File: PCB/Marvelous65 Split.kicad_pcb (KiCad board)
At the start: 2 copper layers, 349.3 x 107.2 mm, 213 parts, among them J1 USB_C_Receptacle_USB2.0, J2 Conn_01x04, J3 AudioJack4, J4 Conn_01x02, J5 USB_C_Receptacle_USB2.0, J6 Conn_01x04, J7 AudioJack4, J8 Conn_01x02, SW1 SW_DPDT_x2, SW2 SW_PUSH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

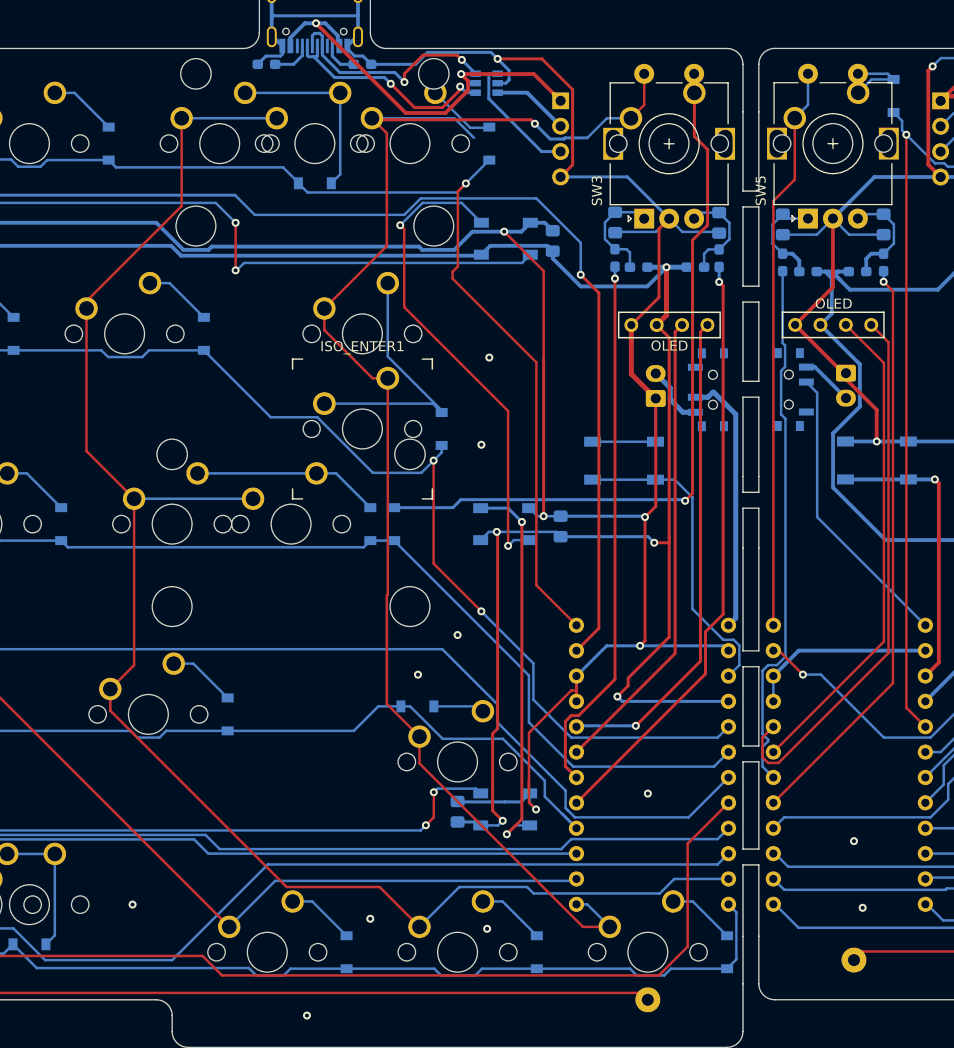
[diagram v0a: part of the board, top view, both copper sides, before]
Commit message: fix iso enter and panelization
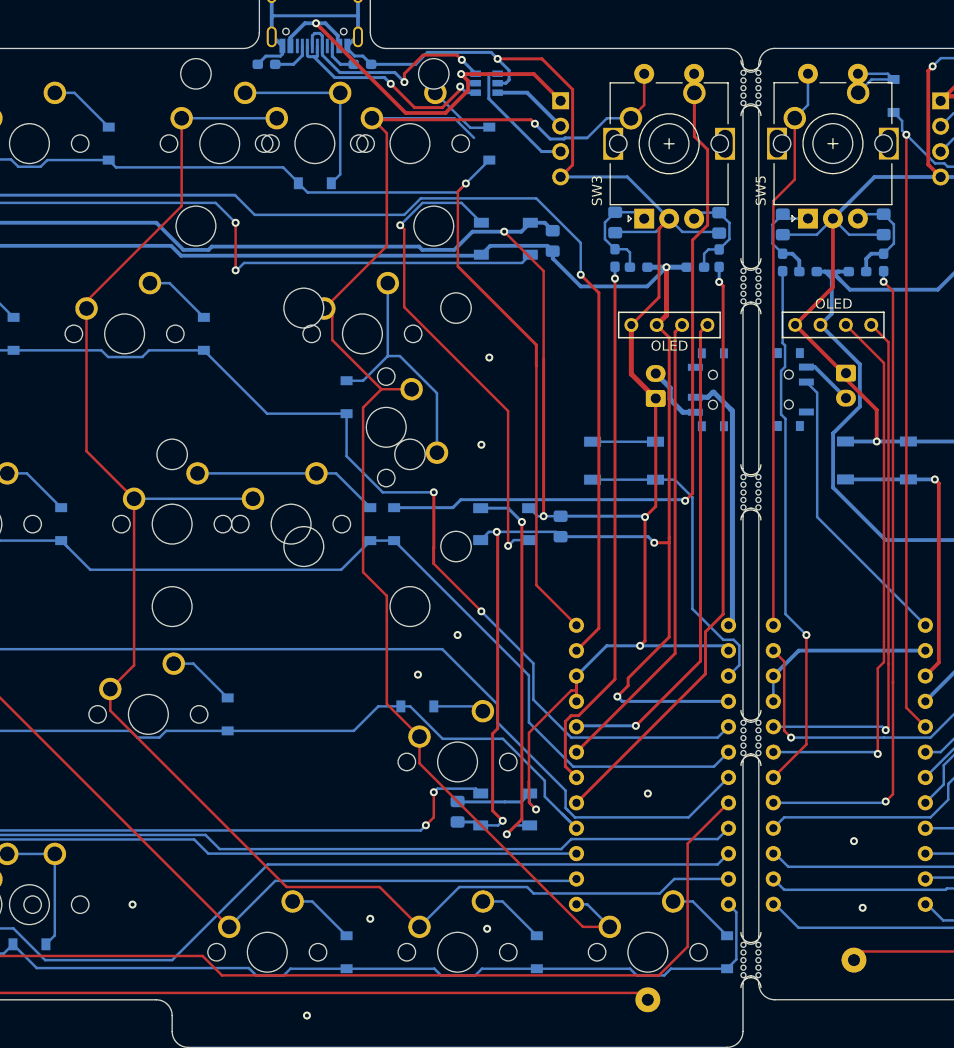
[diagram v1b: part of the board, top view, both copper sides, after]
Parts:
- added mouse-bite-3mm-slot: VAL**, Panelization:mouse-bite-3mm-slot, F.Cu at (-23.4, -114.7)
- added mouse-bite-3mm-slot: VAL**, Panelization:mouse-bite-3mm-slot, F.Cu at (-23.4, -49.6)
- added mouse-bite-3mm-slot: VAL**, Panelization:mouse-bite-3mm-slot, F.Cu at (-23.4, -74.2)
- added mouse-bite-3mm-slot: VAL**, Panelization:mouse-bite-3mm-slot, F.Cu at (-23.4, -94.8)
- added mouse-bite-3mm-slot: VAL**, Panelization:mouse-bite-3mm-slot, F.Cu at (-23.4, -27.4)
- ISO_ENTER1: footprint keyswitches:SW_MX -> MX_Only:MXOnly-ISO-ROTATED-ReversedStabilizers-NoLED
- moved D37 10.0 mm to (-63.9, -83.7)
- moved ISO_ENTER1 2.39 mm to (-59.9, -80.7)
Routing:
- net L_ROT_B: track 58.6 -> 65.2 mm, vias 1 -> 2
- net L_SCL: track 48.9 -> 55.3 mm, vias 0 -> 1
- net L_DATA: track 191.4 -> 196.0 mm
- net ROW2: track 178.2 -> 181.9 mm
- net COL7: track 146.5 -> 149.8 mm
- net Net-(D37-Pad2): track 27.3 -> 24.9 mm
- net ROW1: track 197.7 -> 195.5 mm
- net L_SDA: track 54.5 -> 52.8 mm, vias 0 -> 1
- net L_ROT_A: track 53.5 -> 53.4 mm, vias 0 -> 1
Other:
- outline, holes or cut-outs redrawn

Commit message: updated rendered images
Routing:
- net GND: vias 48 -> 58
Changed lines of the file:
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@@
     (thickness 1.6)
     (drawings 2718)
-    (tracks 1812)
+    (tracks 1822)
     (zones 0)
     (modules 218)
@@
       (padsonsilk false)
       (subtractmaskfromsilk false)
-      (outputformat 1)
+      (outputformat 5)
       (mirror false)
       (drillshape 0)
@@
   (via (at 0.237615 -32.795405) (size 0.8) (drill 0.4) (layers F.Cu B.Cu) (net 2))
   (via (at 5.137615 -50.445405) (size 0.8) (drill 0.4) (layers F.Cu B.Cu) (net 2))
+  (via (at -15.462385 -82.132905) (size 0.8) (drill 0.4) (layers F.Cu B.Cu) (net 2))
+  (via (at -13.081135 -45.620405) (size 0.8) (drill 0.4) (layers F.Cu B.Cu) (net 2))
+  (via (at -31.337385 -48.001655) (size 0.8) (drill 0.4) (layers F.Cu B.Cu) (net 2))
+  (via (at -34.512385 -32.126655) (size 0.8) (drill 0.4) (layers F.Cu B.Cu) (net 2))
+  (via (at -34.512385 -35.301655) (size 0.8) (drill 0.4) (layers F.Cu B.Cu) (net 2))
+  (via (at -34.512385 -38.476655) (size 0.8) (drill 0.4) (layers F.Cu B.Cu) (net 2))
+  (via (at -32.131135 -40.857905) (size 0.8) (drill 0.4) (layers F.Cu B.Cu) (net 2))
+  (via (at 51.212615 -38.476655) (size 0.8) (drill 0.4) (layers F.Cu B.Cu) (net 2))
+  (via (at 21.843865 -55.145405) (size 0.8) (drill 0.4) (layers F.Cu B.Cu) (net 2))
+  (via (at 45.656365 -51.176655) (size 0.8) (drill 0.4) (layers F.Cu B.Cu) (net 2))
   (segment (start -37.01055 -96.785575) (end -37.01055 -95.599325) (width 0.3) (layer B.Cu) (net 3))
   (segment (start -37.0018 -95.608075) (end -37.01055 -95.599325) (width 0.3) (layer B.Cu) (net 3))

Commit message: add schematic and gerber
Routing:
- net GND: vias 58 -> 59
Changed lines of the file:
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@@
     (thickness 1.6)
     (drawings 2718)
-    (tracks 1822)
+    (tracks 1823)
     (zones 0)
     (modules 218)
@@
       (padsonsilk false)
       (subtractmaskfromsilk false)
-      (outputformat 5)
+      (outputformat 1)
       (mirror false)
       (drillshape 0)
@@
   (via (at 21.843865 -55.145405) (size 0.8) (drill 0.4) (layers F.Cu B.Cu) (net 2))
   (via (at 45.656365 -51.176655) (size 0.8) (drill 0.4) (layers F.Cu B.Cu) (net 2))
+  (via (at -161.512385 -43.239155) (size 0.8) (drill 0.4) (layers F.Cu B.Cu) (net 2))
   (segment (start -37.01055 -96.785575) (end -37.01055 -95.599325) (width 0.3) (layer B.Cu) (net 3))
   (segment (start -37.0018 -95.608075) (end -37.01055 -95.599325) (width 0.3) (layer B.Cu) (net 3))

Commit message: update breakout method
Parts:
- removed mouse-bite-3mm-slot (x5): VAL**, Panelization:mouse-bite-3mm-slot
- added REF**: breakaway-mousebites, random-keyboard-parts:breakaway-mousebites, F.Cu at (151.2, -52.0)
- added REF**: breakaway-mousebites, random-keyboard-parts:breakaway-mousebites, F.Cu at (134.6, -109.1)
- added REF**: breakaway-mousebites, random-keyboard-parts:breakaway-mousebites, F.Cu at (139.3, -52.0)
- added REF**: breakaway-mousebites, random-keyboard-parts:breakaway-mousebites, F.Cu at (151.2, -32.9)
- added REF**: breakaway-mousebites, random-keyboard-parts:breakaway-mousebites, F.Cu at (139.3, -32.9)
- added REF**: breakaway-mousebites, random-keyboard-parts:breakaway-mousebites, F.Cu at (141.7, -71.0)
- added REF**: breakaway-mousebites, random-keyboard-parts:breakaway-mousebites, F.Cu at (129.8, -71.0)
- added REF**: breakaway-mousebites, random-keyboard-parts:breakaway-mousebites, F.Cu at (125.0, -90.1)
- added REF**: breakaway-mousebites, random-keyboard-parts:breakaway-mousebites, F.Cu at (136.9, -90.1)
- added REF**: breakaway-mousebites, random-keyboard-parts:breakaway-mousebites, F.Cu at (146.5, -109.1)
- moved J3 346.9 mm to (165.5, -117.9)
- moved C2 346.9 mm to (294.1, -42.2)
- moved D28 346.9 mm to (283.0, -28.1)
- moved D35 346.9 mm to (302.0, -28.1)
- moved D39 346.9 mm to (290.1, -52.8)
- moved D43 346.9 mm to (298.9, -99.6)
- moved D45 346.9 mm to (298.9, -71.0)
- moved J4 346.9 mm to (313.9, -83.6)
- moved K_BSPC2 346.9 mm to (270.3, -109.1)
- moved K_DOWN1 346.9 mm to (294.1, -28.1)
- moved K_UP1 346.9 mm to (294.1, -47.2)
- moved R3 346.9 mm to (309.9, -97.7)
- moved R4 346.9 mm to (312.2, -96.7)
- moved R5 346.9 mm to (317.9, -96.7)
- moved SW2 346.9 mm to (310.8, -77.4)
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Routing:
- net L_ROW2: track 147.2 -> 137.9 mm
- net L_ROW3: track 152.6 -> 143.3 mm
- net L_ROW0: track 208.5 -> 199.3 mm
- net L_ROW1: track 163.1 -> 154.0 mm
- net L_ROW4: track 160.8 -> 151.7 mm
- net GND: track 1095.8 -> 1092.8 mm, vias 59 -> 60
- net Net-(D81-Pad2): track 6.82 -> 9.44 mm
- net Net-(D77-Pad2): track 6.82 -> 9.44 mm
- net Net-(D80-Pad2): track 6.82 -> 9.41 mm
- net Net-(D79-Pad2): track 6.82 -> 9.39 mm
- net Net-(D76-Pad2): track 6.82 -> 9.39 mm
- net VCC: track 926.8 -> 925.0 mm
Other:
- board size 349.3 x 107.2 mm -> 345.3 x 107.2 mm
